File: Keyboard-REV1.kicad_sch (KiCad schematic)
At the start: 16 parts, among them J1 USB_mini_micro_B, SW1 SW_PUSH, U1 ATMEGA32U4, X1 XTAL_GND

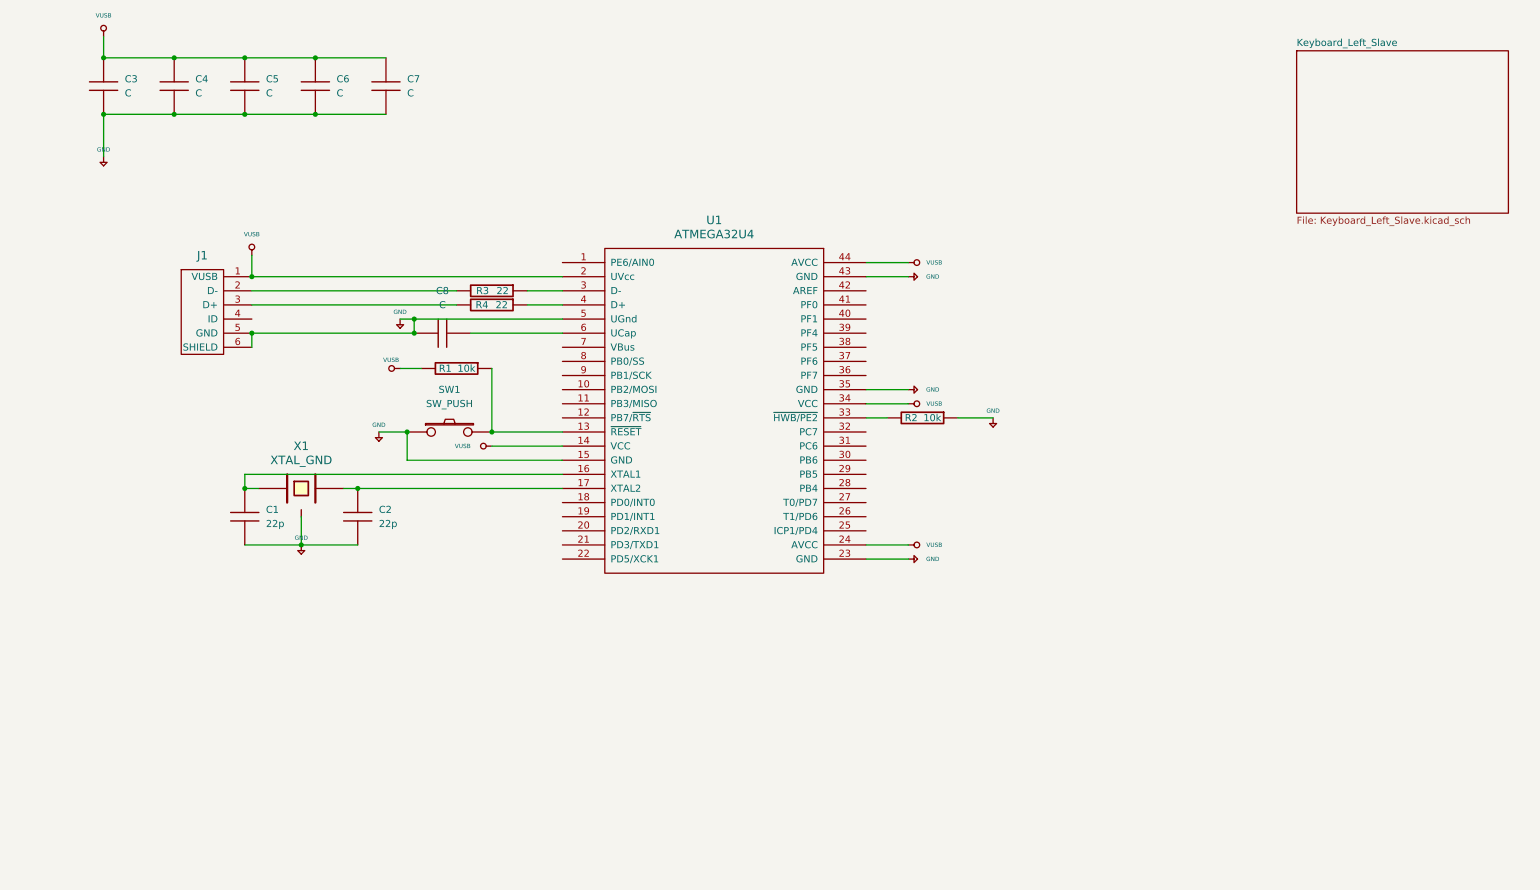
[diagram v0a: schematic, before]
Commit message: Added key matrix
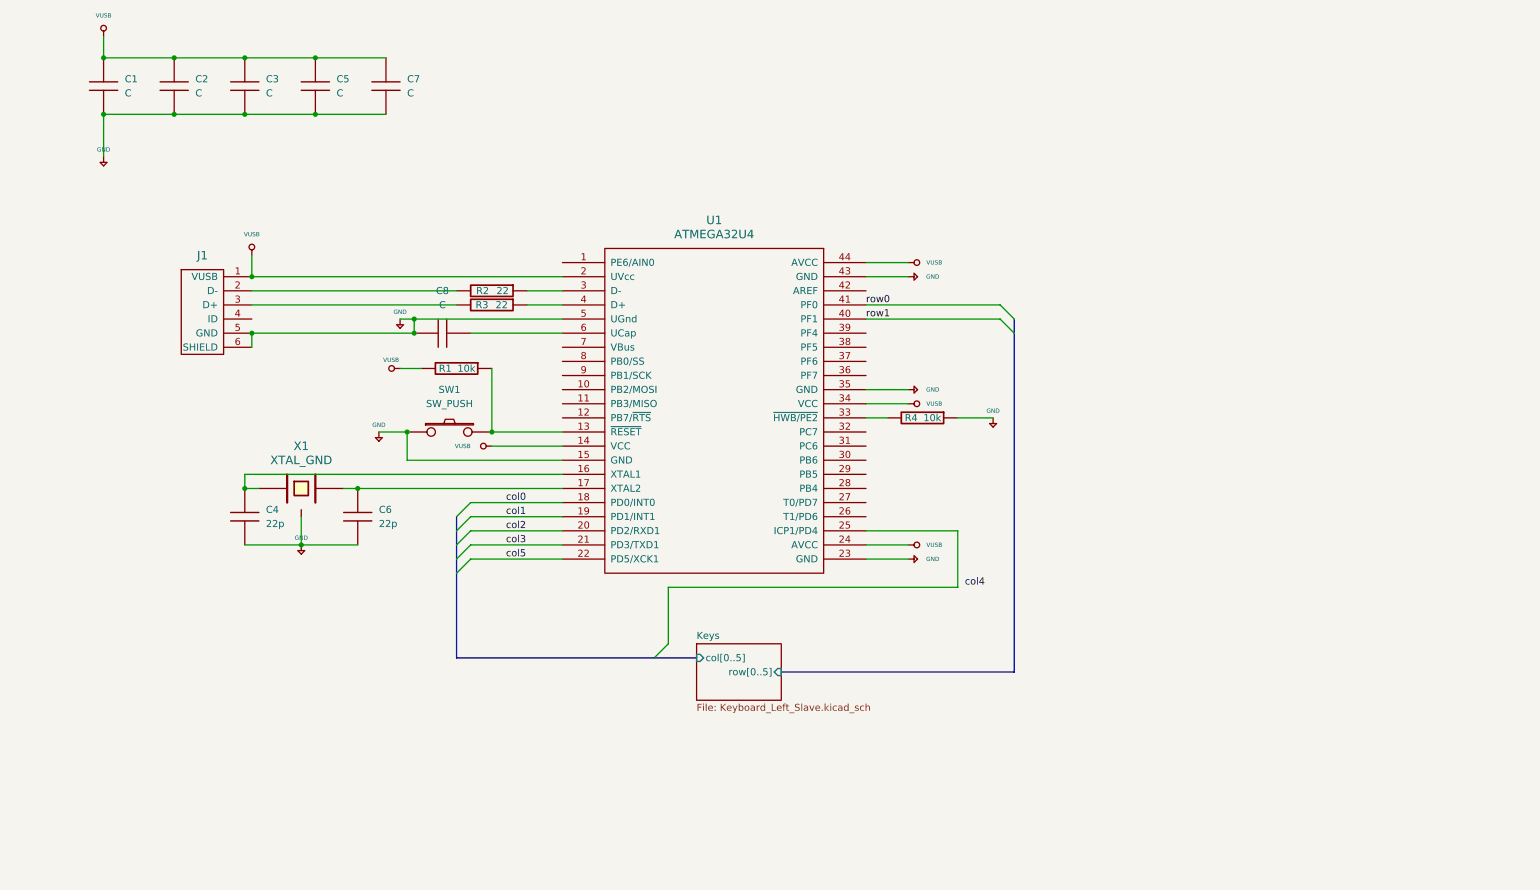
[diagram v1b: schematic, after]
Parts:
- C1: renamed from C3; footprint (none) -> Capacitor_SMD:C_0805_2012Metric
- C2: renamed from C4; footprint (none) -> Capacitor_SMD:C_0805_2012Metric
- C3: renamed from C5; footprint (none) -> Capacitor_SMD:C_0805_2012Metric
- C4: renamed from C1; footprint (none) -> Capacitor_SMD:C_0805_2012Metric
- C5: renamed from C6; footprint (none) -> Capacitor_SMD:C_0805_2012Metric
- C6: renamed from C2; footprint (none) -> Capacitor_SMD:C_0805_2012Metric
- C7, C8: footprint (none) -> Capacitor_SMD:C_0805_2012Metric
- J1: footprint (none) -> keyboard_parts:USB_miniB_hirose_5S8
- R1: footprint (none) -> Resistor_SMD:R_0805_2012Metric_Pad1.20x1.40mm_HandSolder
- R2: renamed from R3; footprint (none) -> Resistor_SMD:R_0805_2012Metric_Pad1.20x1.40mm_HandSolder
- R3: renamed from R4; footprint (none) -> Resistor_SMD:R_0805_2012Metric_Pad1.20x1.40mm_HandSolder
- R4: renamed from R2; footprint (none) -> Resistor_SMD:R_0805_2012Metric_Pad1.20x1.40mm_HandSolder
- U1: footprint (none) -> Package_QFP:TQFP-44_10x10mm_P0.8mm
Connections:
- net col0: now reaches U1.18 (PD0/INT0)
- net col1: now reaches U1.19 (PD1/INT1)
- net col2: now reaches U1.20 (PD2/RXD1)
- net col3: now reaches U1.21 (PD3/TXD1)
- net col5: now reaches U1.22 (PD5/XCK1)
- net row1: now reaches U1.40 (PF1)
- net row0: now reaches U1.41 (PF0)
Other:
- sheet Keyboard_Left_Slave renamed Keys
- sheet Keys ports: added col[0..5], row[0..5]; removed none

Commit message: Changed to STM32H5
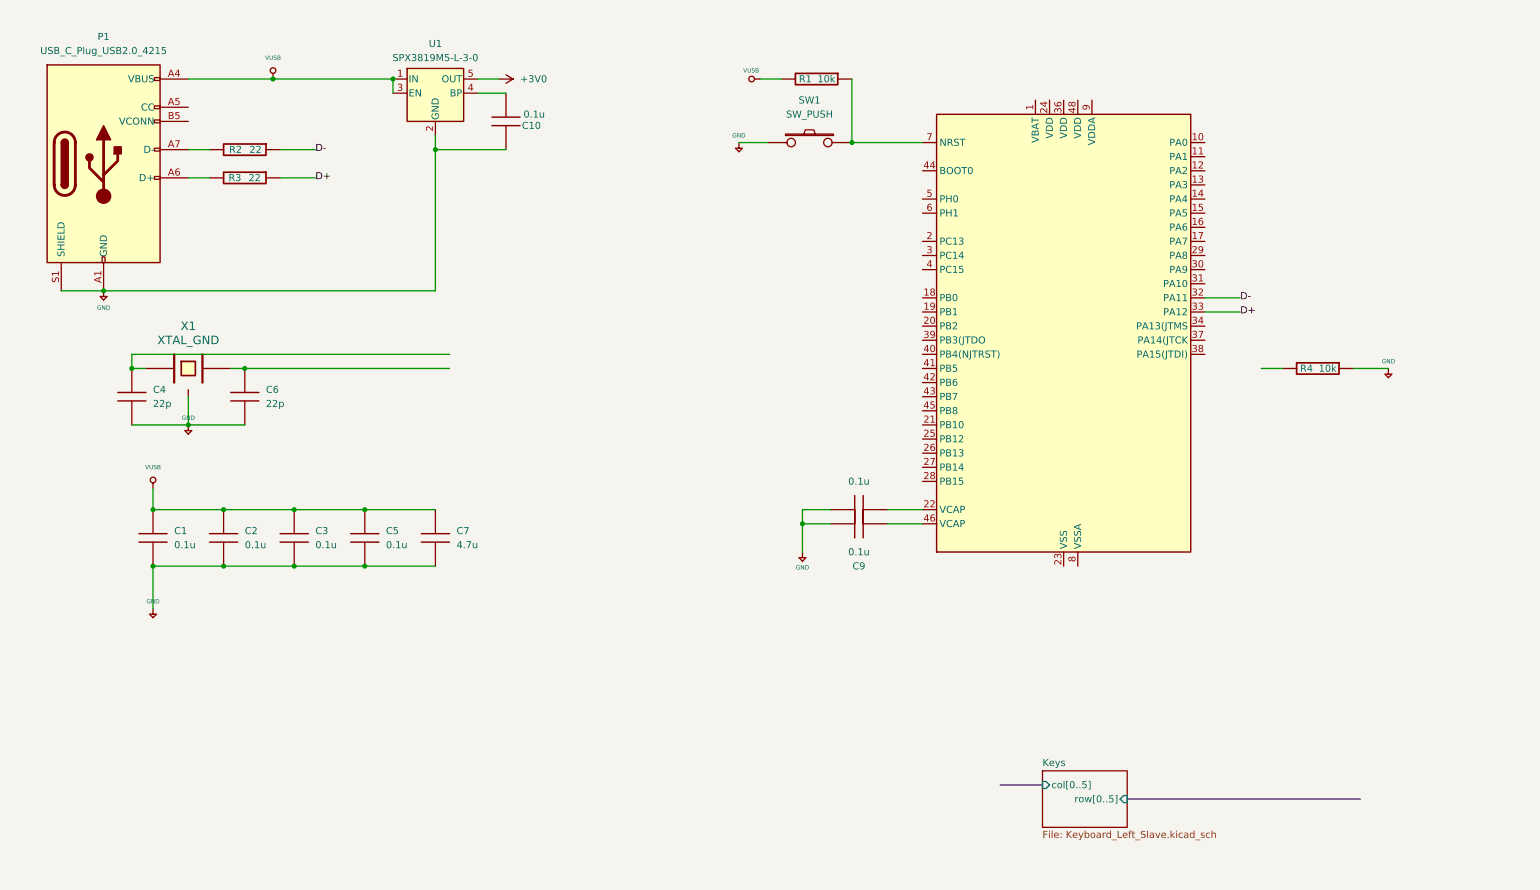
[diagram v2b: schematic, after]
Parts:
- removed J1: USB_mini_micro_B, keyboard_parts:USB_miniB_hirose_5S8, symbol keyboard_parts:USB_mini_micro_B
- removed U1: ATMEGA32U4, Package_QFP:TQFP-44_10x10mm_P0.8mm, symbol keyboard_parts:ATMEGA32U4
- added C10, C9: 0.1u, Capacitor_SMD:C_0805_2012Metric, symbol keyboard_parts:C
- added P1: USB_C_Plug_USB2.0_4215, symbol Connector:USB_C_Plug_USB2.0
- added U1: SPX3819M5-L-3-0, Package_TO_SOT_SMD:SOT-23-5, symbol Regulator_Linear:SPX3819M5-L-3-0
- added U2: STM32H503CBTx, Package_QFP:LQFP-48_7x7mm_P0.5mm, symbol MCU_ST_STM32H5:STM32H503CBTx
- C1, C2, C3, C5, C8: value C -> 0.1u
- C7: value C -> 4.7u
- SW1: footprint (none) -> Button_Switch_THT:SW_PUSH_6mm
- X1: footprint (none) -> Crystal:Crystal_SMD_3225-4Pin_3.2x2.5mm_HandSoldering
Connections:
- net GND: now also C10.2, C9.2, P1.A1 (GND), P1.A12 (GND), P1.B1 (GND), P1.B12 (GND), P1.S1 (SHIELD), U1.2 (GND)
- net VUSB: now also P1.A4 (VBUS), P1.A9 (VBUS), P1.B4 (VBUS), P1.B9 (VBUS), U1.1 (IN), U1.3 (EN)
- net at C8.2: now also U2.22 (VCAP)
- net at R1.1, SW1.2: now also U2.7 (NRST)
- net D-: now reaches R2.1
- net D-: now also U2.32 (PA11)
- net at R2.2: now also P1.A7 (D-)
- net D+: now reaches R3.1
- net D+: now also U2.33 (PA12)
- net at R3.2: now also P1.A6 (D+)
- new net: C9.1, U2.46 (VCAP)
- new net: C10.1, U1.4 (BP)
- new net: U2.23 (VSS), U2.35 (VSS), U2.47 (VSS)
- new net +3V0: U1.5 (OUT)
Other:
- moved on the sheet: C1, C2, C3, C4, C5, C6, C7, R1, R2, R3, R4, SW1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

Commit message: Added JTAG, corrected connections for stm32h5
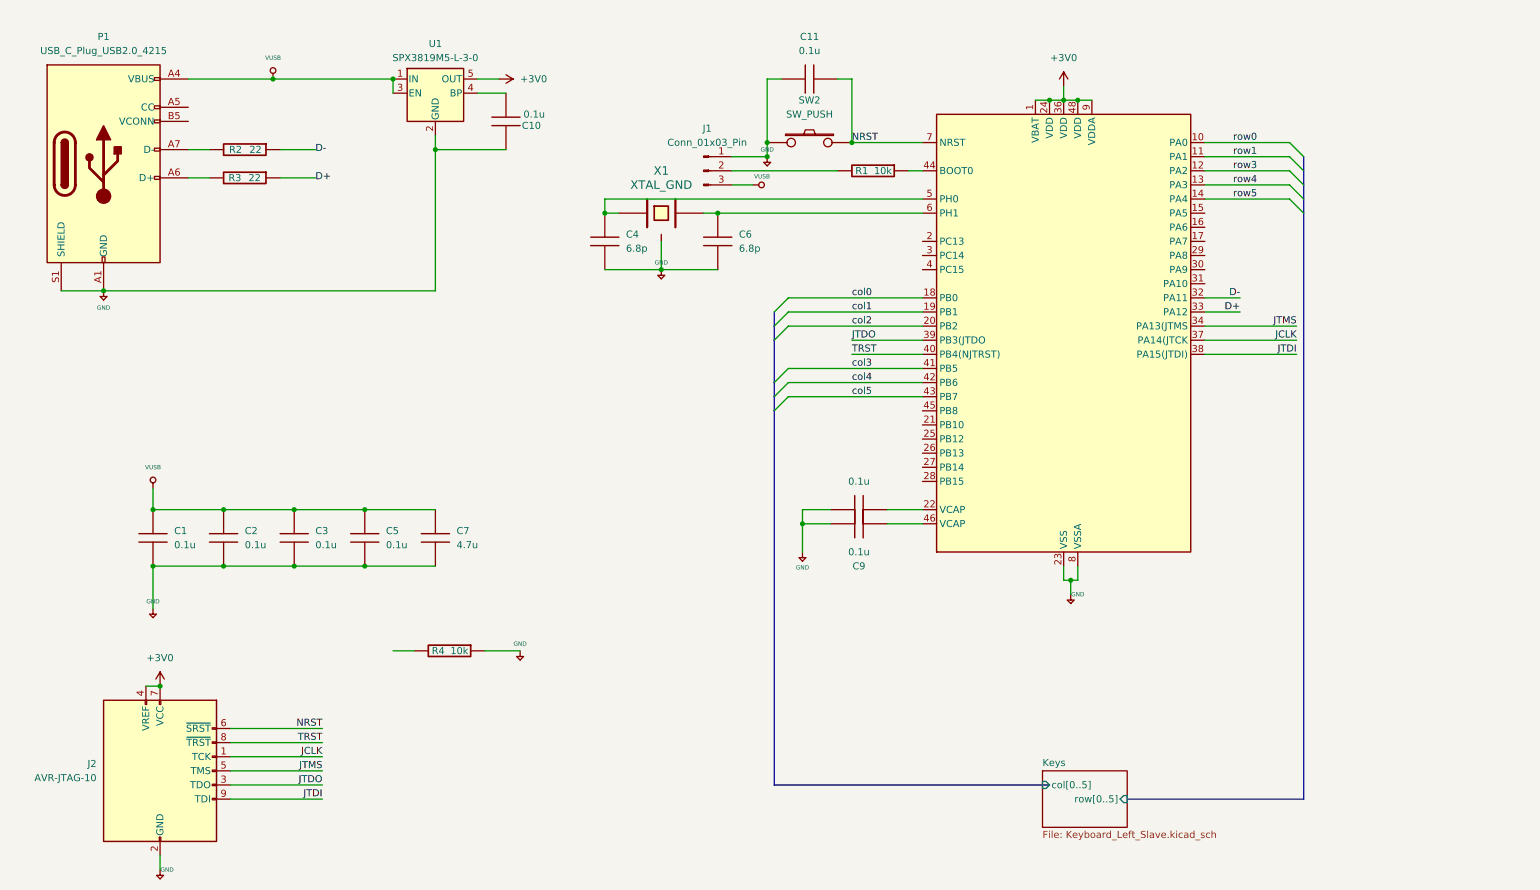
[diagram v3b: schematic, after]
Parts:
- removed SW1: SW_PUSH, Button_Switch_THT:SW_PUSH_6mm, symbol keyboard_parts:SW_PUSH
- added C11: 0.1u, Capacitor_SMD:C_0805_2012Metric, symbol keyboard_parts:C
- added J1: Conn_01x03_Pin, symbol Connector:Conn_01x03_Pin
- added J2: AVR-JTAG-10, symbol Connector:AVR-JTAG-10
- added SW2: SW_PUSH, Button_Switch_THT:SW_PUSH_6mm, symbol keyboard_parts:SW_PUSH
- C4, C6: value 22p -> 6.8p
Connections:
- net +3V0: now also U2.1 (VBAT), U2.24 (VDD), U2.36 (VDD), U2.48 (VDD), U2.9 (VDDA), J2.4 (VREF), J2.7 (VCC)
- net GND: now also U2.23 (VSS), U2.35 (VSS), U2.47 (VSS), U2.8 (VSSA), C11.1, J1.1 (Pin_1), J2.10 (GND), J2.2 (GND), SW2.1
- net VUSB: now also J1.3 (Pin_3); no longer R1.2
- net at C4.1, X1.1: now also U2.5 (PH0)
- net at C6.1, X1.2: now also U2.6 (PH1)
- net at R1.1: now also U2.44 (BOOT0); no longer U2.7 (NRST)
- net row0: now reaches U2.10 (PA0)
- net row1: now reaches U2.11 (PA1)
- net row3: now reaches U2.12 (PA2)
- net row4: now reaches U2.13 (PA3)
- net row5: now reaches U2.14 (PA4)
- net col0: now reaches U2.18 (PB0)
- net col1: now reaches U2.19 (PB1)
- net col2: now reaches U2.20 (PB2)
- net JTMS: now reaches U2.34 (PA13(JTMS)
- net JTMS: now also J2.5 (TMS)
- net JCLK: now reaches U2.37 (PA14(JTCK)
- net JCLK: now also J2.1 (TCK)
- net JTDI: now reaches U2.38 (PA15(JTDI))
- net JTDI: now also J2.9 (TDI)
- net JTDO: now reaches U2.39 (PB3(JTDO)
- net JTDO: now also J2.3 (TDO)
- net TRST: now reaches U2.40 (PB4(NJTRST))
- net TRST: now also J2.8 (~{TRST})
- net col3: now reaches U2.41 (PB5)
- net col4: now reaches U2.42 (PB6)
- net col5: now reaches U2.43 (PB7)
- new net: J1.2 (Pin_2), R1.2
- new net NRST: C11.2, J2.6 (~{SRST}), SW2.2, U2.7 (NRST)
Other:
- moved on the sheet: C4, C6, R1, R4, X1

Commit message: Changed to STM32L412
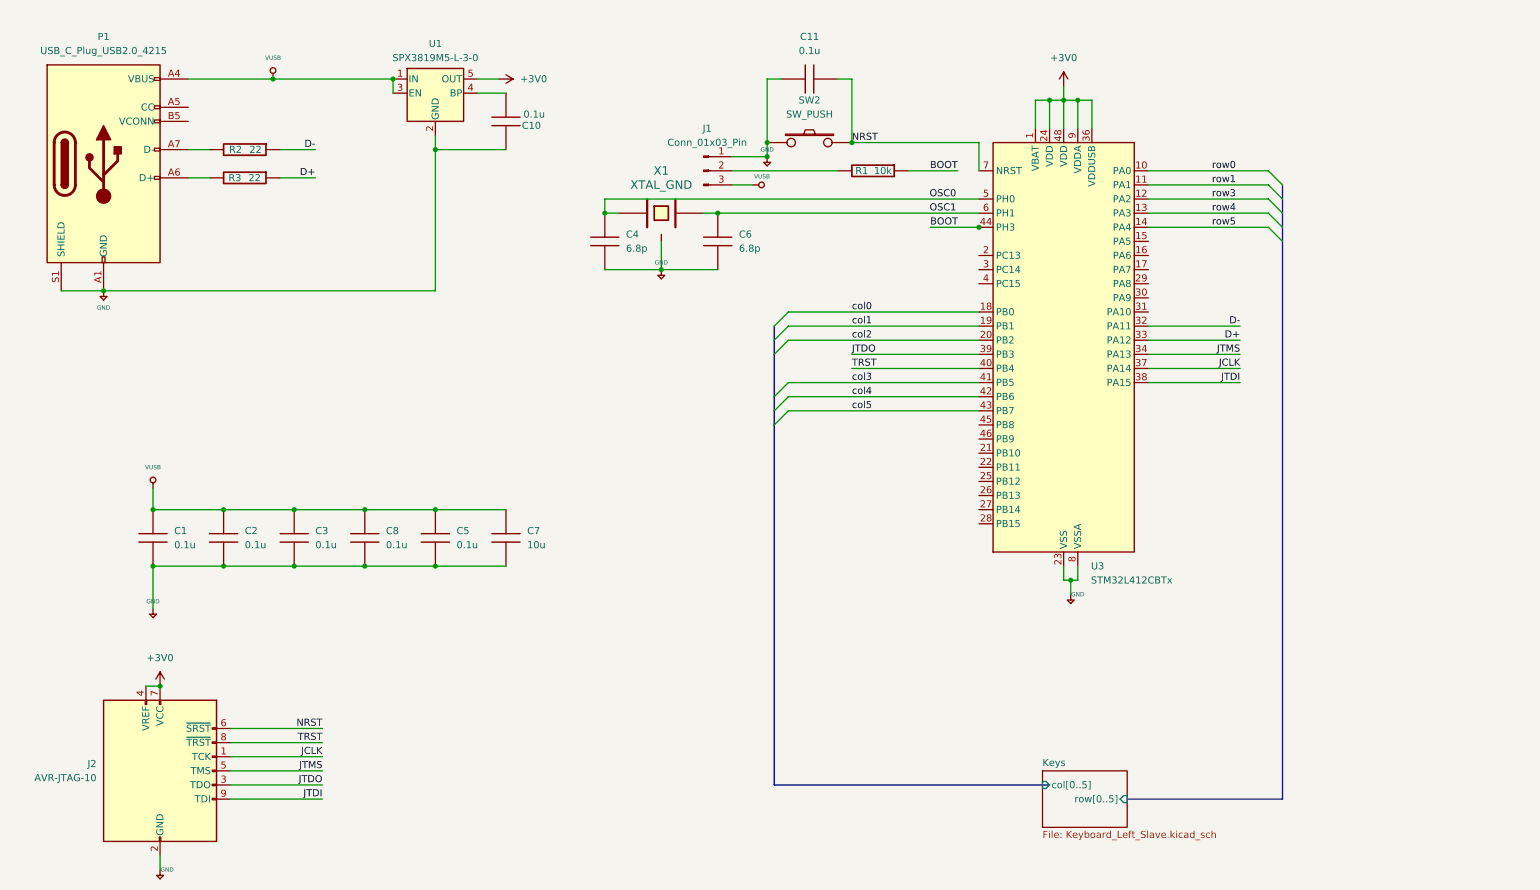
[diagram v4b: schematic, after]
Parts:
- removed C9: 0.1u, Capacitor_SMD:C_0805_2012Metric, symbol keyboard_parts:C
- removed R4: 10k, Resistor_SMD:R_0805_2012Metric_Pad1.20x1.40mm_HandSolder, symbol keyboard_parts:R
- removed U2: STM32H503CBTx, Package_QFP:LQFP-48_7x7mm_P0.5mm, symbol MCU_ST_STM32H5:STM32H503CBTx
- added U3: STM32L412CBTx, Package_QFP:LQFP-48_7x7mm_P0.5mm, symbol MCU_ST_STM32L4:STM32L412CBTx
- C7: value 4.7u -> 10u
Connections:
- net +3V0: now also U3.1 (VBAT), U3.24 (VDD), U3.36 (VDDUSB), U3.48 (VDD), U3.9 (VDDA)
- net D+: now also U3.33 (PA12)
- net D-: now also U3.32 (PA11)
- net GND: now also C8.2, U3.23 (VSS), U3.35 (VSS), U3.47 (VSS), U3.8 (VSSA); no longer C8.1
- net JCLK: now also U3.37 (PA14)
- net JTDI: now also U3.38 (PA15)
- net JTDO: now also U3.39 (PB3)
- net JTMS: now also U3.34 (PA13)
- net NRST: now also U3.7 (NRST)
- net TRST: now also U3.40 (PB4)
- net VUSB: now also C8.1
- net col0: now also U3.18 (PB0)
- net col1: now also U3.19 (PB1)
- net col2: now also U3.20 (PB2)
- net col3: now also U3.41 (PB5)
- net col4: now also U3.42 (PB6)
- net col5: now also U3.43 (PB7)
- net row0: now also U3.10 (PA0)
- net row1: now also U3.11 (PA1)
- net row3: now also U3.12 (PA2)
- net row4: now also U3.13 (PA3)
- net row5: now also U3.14 (PA4)
- net OSC0: now reaches C4.1, X1.1
- net OSC0: now also U3.5 (PH0)
- net OSC1: now reaches C6.1, X1.2
- net OSC1: now also U3.6 (PH1)
- net BOOT: now reaches R1.1
- net BOOT: now also U3.44 (PH3)
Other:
- moved on the sheet: C5, C7
